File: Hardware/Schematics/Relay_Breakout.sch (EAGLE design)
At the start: 63 parts, among them U1 ESP-32S

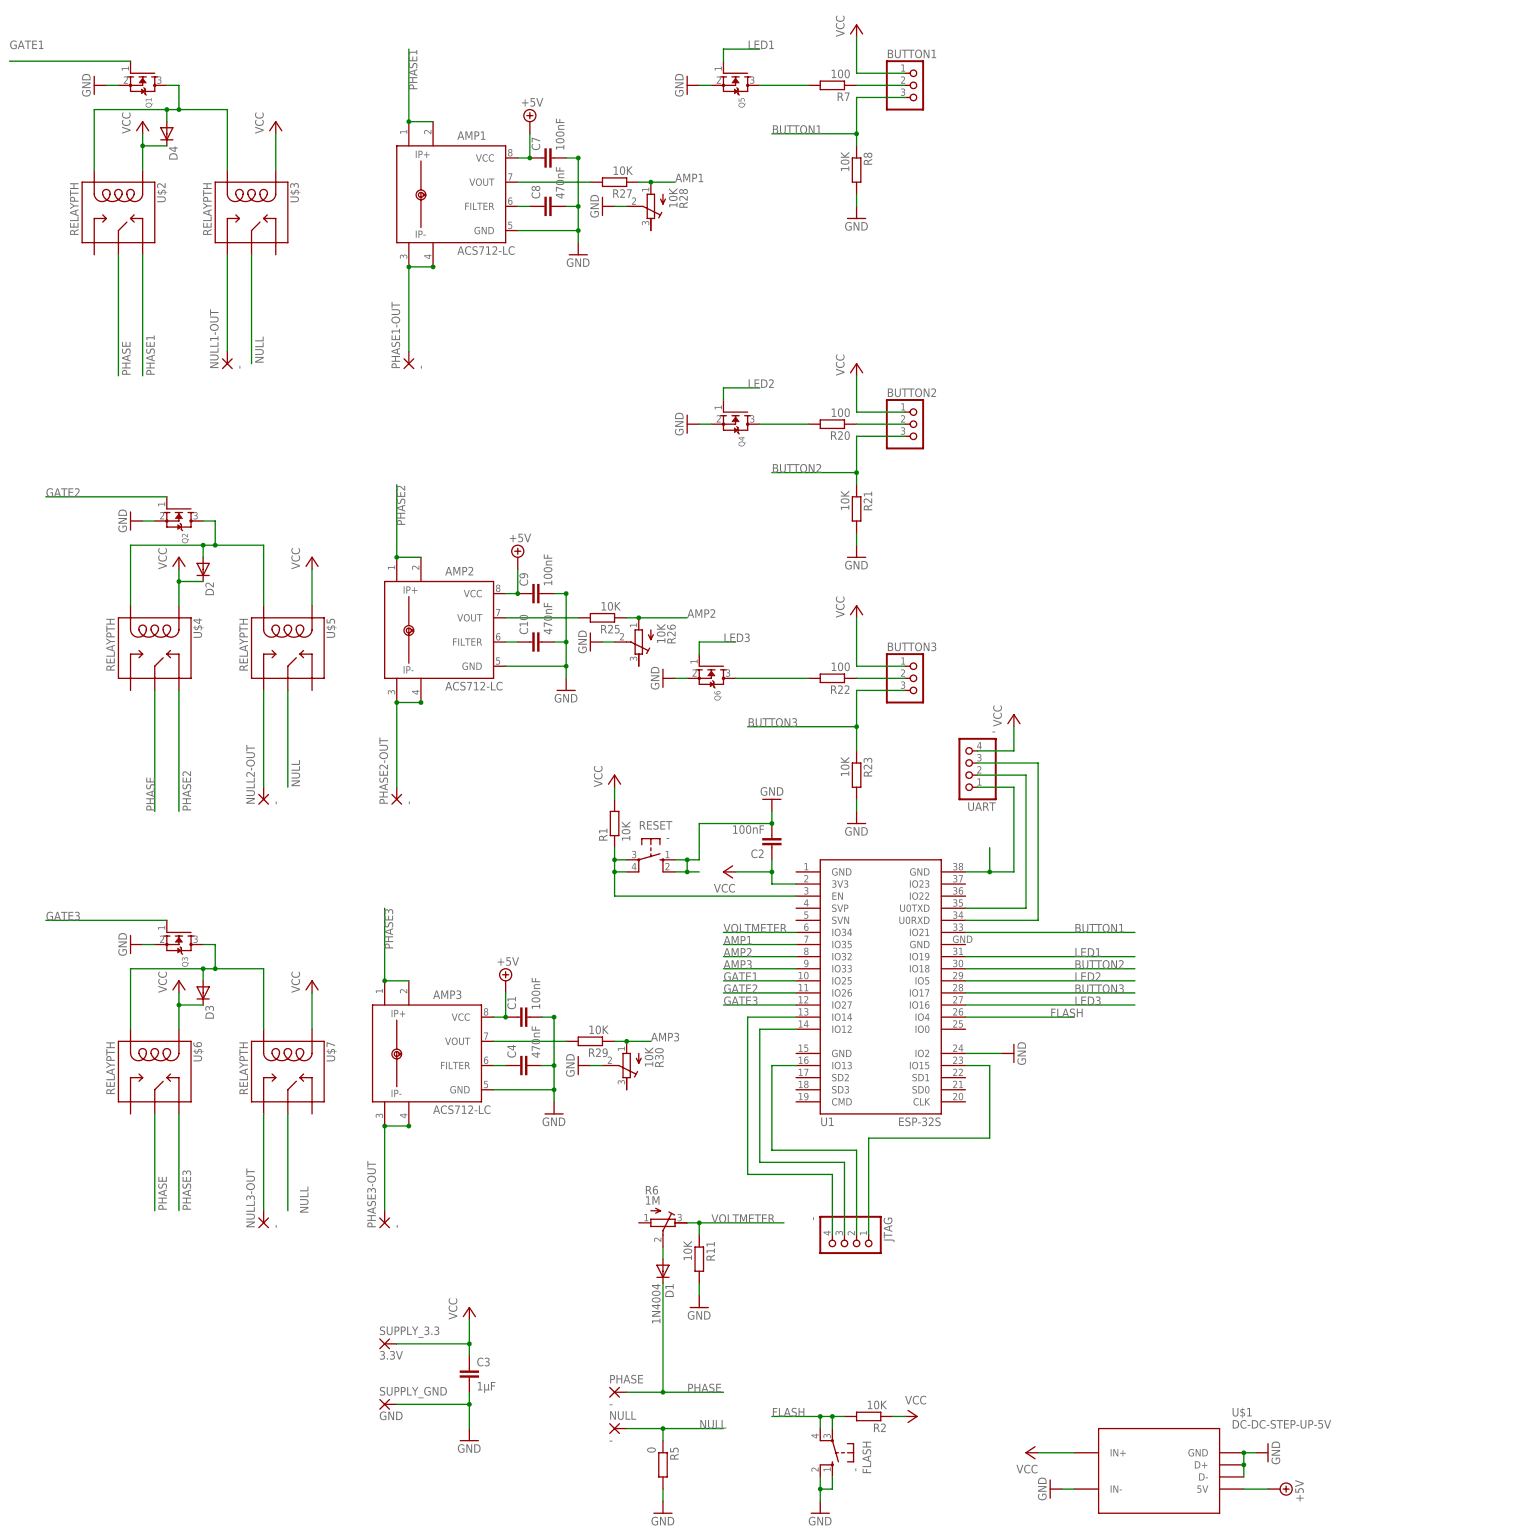
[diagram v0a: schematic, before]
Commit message: Made relay and amperemeter breakout board.
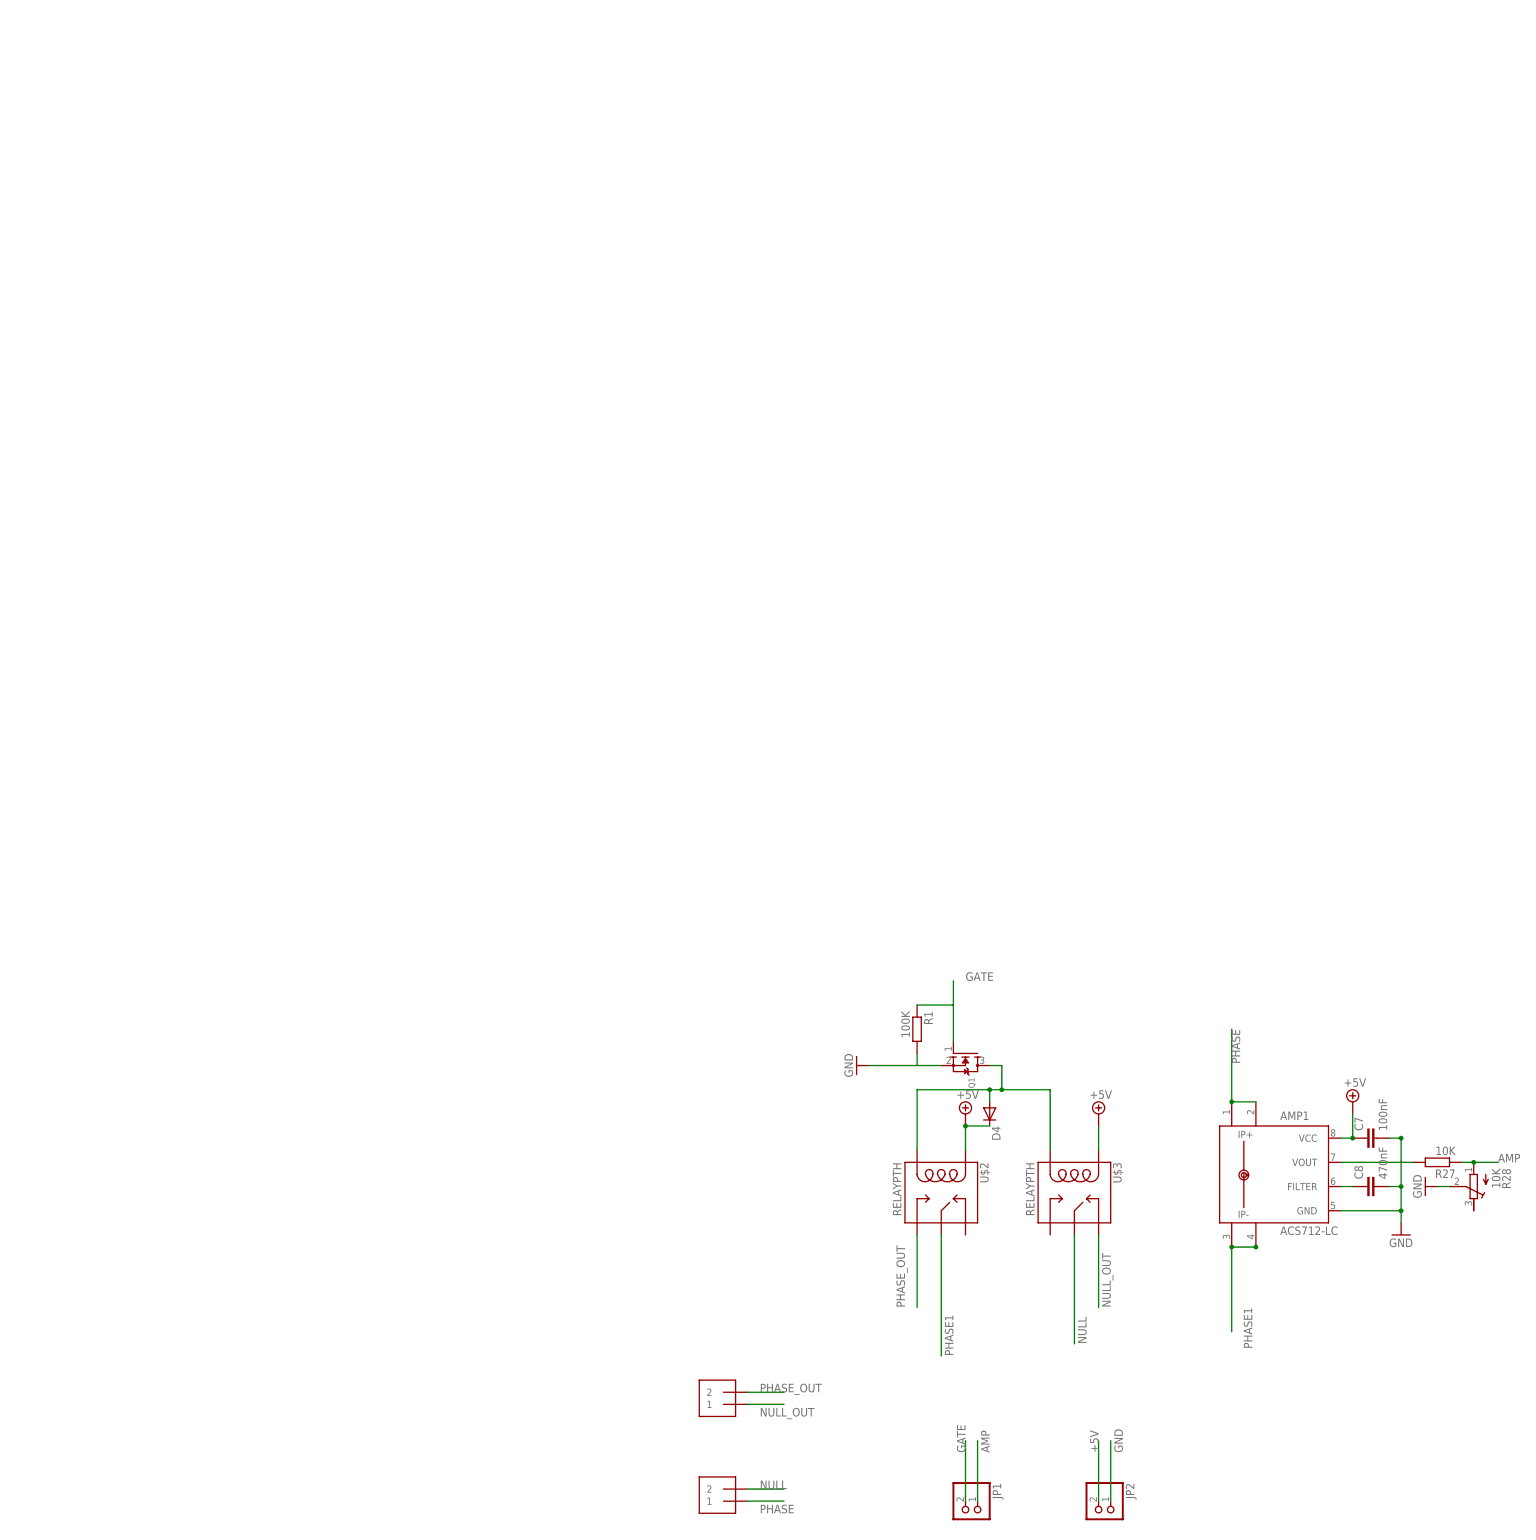
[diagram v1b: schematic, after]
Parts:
- removed AMP2, AMP3: ACS712-LC, allegro-2:ACS712-LC
- removed BUTTON1, BUTTON2, BUTTON3: (no value), pinhead:PINHD-1X3
- removed C1, C9: 100nF, rcl:C-EUC0805
- removed C10, C4: 470nF, rcl:C-EUC0805
- removed C2: 100nF, rcl:C-EUC1206
- removed C3: 1µF, rcl:C-EU025-024X044
- removed D1: 1N4004, diode:1N4004
- removed D2, D3: (no value), diode:DIODE-DO-214AC
- removed FLASH, RESET: -, switch-omron:10-XX
- removed JTAG, UART: -, pinhead:PINHD-1X4
- removed NULL, NULL1-OUT, NULL2-OUT, NULL3-OUT, PHASE, PHASE1-OUT, PHASE2-OUT, PHASE3-OUT: -, wirepad:3,81/1,4
- removed Q2, Q3, Q4, Q5, Q6: (no value), adafruit:MOSFET-NREFLOW
- removed R11, R2, R21, R23, R25, R29, R8: 10K, rcl:R-EU_R0805
- removed R20, R22, R7: 100, rcl:R-EU_R0805
- removed R26, R30: 10K, rcl:R-TRIMM5X
- removed R5: 0, eagle-ltspice:RR2010
- removed R6: 1M, rcl:R-TRIMM3296W
- removed SUPPLY_3.3: 3.3V, wirepad:2,15/1,0
- removed SUPPLY_GND: GND, wirepad:2,15/1,0
- removed U$1: DC-DC-STEP-UP-5V, diy-modules:DC-DC-STEP-UP-5V
- removed U$4, U$5, U$6, U$7: RELAYPTH, SRD-05VDC-SL-C:RELAYPTH
- removed U1: ESP-32S, esp32:ESP-32S
- added J1, J2: 1X2-3.5MM, adafruit:1X2-3.5MM
- added JP1, JP2: (no value), pinhead:PINHD-1X2
- R1: value 10K -> 100K
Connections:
- removed net AMP1: R27.1, R28.A, U1.IO35
- removed net AMP2: R25.1, R26.A, U1.IO32
- removed net AMP3: R29.1, R30.A, U1.IO33
- removed net BUTTON1: BUTTON1.3, R8.1, U1.IO21
- removed net BUTTON2: BUTTON2.3, R21.1, U1.IO18
- removed net BUTTON3: BUTTON3.3, R23.1, U1.IO17
- removed net FLASH: FLASH.P, FLASH.P1, R2.2, U1.IO4
- removed net GATE1: Q1.G, U1.IO25
- removed net GATE2: Q2.G, U1.IO26
- removed net GATE3: Q3.G, U1.IO27
- removed net LED1: Q5.G, U1.IO19
- removed net LED1_SWITCHED: Q5.D, R7.2
- removed net LED2: Q4.G, U1.IO5
- removed net LED2_SWITCHED: Q4.D, R20.2
- removed net LED3: Q6.G, U1.IO16
- removed net LED3_SWITCHED: Q6.D, R22.2
- removed net N$10: AMP3.IP-, AMP3.IP-1, PHASE3-OUT.P
- removed net N$11: BUTTON3.2, R22.1
- removed net N$12: AMP2.IP-, AMP2.IP-1, PHASE2-OUT.P
- removed net N$13: AMP2.FILTER, C10.1
- removed net N$14: D2.A, Q2.D, U$4.COIL0, U$5.COIL0
- removed net N$17: NULL2-OUT.P, U$5.SWOPEN
- removed net N$19: U1.GND@3, UART.1
- removed net N$26: AMP3.FILTER, C4.1
- removed net N$27: AMP1.IP-, AMP1.IP-1, PHASE1-OUT.P
- removed net N$3: JTAG.2, U1.IO13
- removed net N$37: AMP3.VOUT, R29.2
- removed net N$39: AMP2.VOUT, R25.2
- removed net N$4: JTAG.3, U1.IO12
- removed net N$42: D1.A, R6.S
- removed net N$5: JTAG.4, U1.IO14
- removed net N$6: D3.A, Q3.D, U$6.COIL0, U$7.COIL0
- removed net N$66: R1.1, RESET.P, RESET.P1, U1.EN
- removed net N$7: BUTTON2.2, R20.1
- removed net N$70: U1.U0TXD, UART.2
- removed net N$77: U1.U0RXD, UART.3
- removed net N$8: NULL1-OUT.P, U$3.SWOPEN
- removed net N$9: BUTTON1.2, R7.1
- removed net NULL_: NULL3-OUT.P, U$7.SWOPEN
- removed net PHASE2: AMP2.IP+, AMP2.IP+1, U$4.SWCLOSE
- removed net PHASE3: AMP3.IP+, AMP3.IP+1, U$6.SWCLOSE
- removed net VCC: BUTTON1.1, BUTTON2.1, BUTTON3.1, C2.1, C3.1, D2.C, D3.C, D4.C, R1.2, R2.1, SUPPLY_3.3.P, U$1.IN+, U$2.COIL1, U$3.COIL1, U$4.COIL1, U$5.COIL1, U$6.COIL1, U$7.COIL1, U1.3V3, UART.4
- removed net VOLTMETER: R11.1, R6.E, U1.IO34
- new net AMP: JP1.1, R27.1, R28.A
- new net GATE: JP1.2, Q1.G, R1.1
- new net NULL_OUT: J2.1, U$3.SWCLOSE
- new net PHASE_OUT: J2.2, U$2.SWOPEN
- net +5V: now also JP2.2, U$3.COIL1; no longer AMP2.VCC, AMP3.VCC, C1.1, C9.1, U$1.5V
- net GND: now also JP2.1, R1.2; no longer AMP2.GND, AMP3.GND, C1.2, C10.2, C2.2, C3.2, C4.2, C9.2, FLASH.S, FLASH.S1, Q2.S, Q3.S, Q4.S, Q5.S, Q6.S, R11.2, R21.2, R23.2, R26.S, R30.S, R5.2, R8.2, RESET.S, RESET.S1, SUPPLY_GND.P, U$1.D+, U$1.D-, U$1.GND, U$1.IN-, U1.IO2
- net N$2: now also D4.C, U$2.COIL1; no longer JTAG.1, U1.IO15
- net NULL: now also J1.2; no longer NULL.P, R5.1, U$5.SWCOMMON, U$7.SWCOMMON
- net PHASE: now also AMP1.IP+, AMP1.IP+1, J1.1; no longer D1.C, PHASE.P, U$2.SWCOMMON, U$4.SWCOMMON, U$6.SWCOMMON
- net PHASE1: now also AMP1.IP-, AMP1.IP-1, U$2.SWCOMMON; no longer AMP1.IP+, AMP1.IP+1, U$2.SWCLOSE
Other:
- moved on the sheet: AMP1, C7, C8, D4, Q1, R1, R27, R28, U$2, U$3

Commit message: fixed some issues in relay breakout.
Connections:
- removed net N$2: D4.C, U$2.COIL1
- net +5V: now also D4.C, U$2.COIL1
- net PHASE_OUT: now also U$2.SWCLOSE; no longer U$2.SWOPEN
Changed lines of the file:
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@@
 <part name="J2" library="adafruit" deviceset="1X2" device="-3.5MM"/>
 <part name="P+1" library="supply2" deviceset="+5V" device=""/>
-<part name="P+2" library="supply2" deviceset="+5V" device=""/>
 <part name="R1" library="rcl" deviceset="R-EU_" device="R0805" value="100K"/>
 <part name="JP1" library="pinhead" deviceset="PINHD-1X2" device=""/>
 <part name="JP2" library="pinhead" deviceset="PINHD-1X2" device=""/>
+<part name="P+2" library="supply2" deviceset="+5V" device=""/>
 </parts>
 <sheets>
@@
 <instance part="J2" gate="G$1" x="-22.86" y="-35.56" rot="R180"/>
 <instance part="P+1" gate="+5V" x="55.88" y="22.86"/>
-<instance part="P+2" gate="+5V" x="27.94" y="22.86"/>
 <instance part="R1" gate="G$1" x="17.78" y="40.64" rot="R270"/>
 <instance part="JP1" gate="G$1" x="27.94" y="-60.96" rot="R270"/>
 <instance part="JP2" gate="G$1" x="55.88" y="-60.96" rot="R270"/>
+<instance part="P+2" gate="+5V" x="27.94" y="22.86"/>
 </instances>
 <busses>
@@
 <wire x1="17.78" y1="33.02" x2="7.62" y2="33.02" width="0.1524" layer="91"/>
 <wire x1="17.78" y1="35.56" x2="17.78" y2="33.02" width="0.1524" layer="91"/>
+<junction x="17.78" y="33.02"/>
 </segment>
 <segment>
@@
 <wire x1="25.4" y1="45.72" x2="25.4" y2="50.8" width="0.1524" layer="91"/>
 <wire x1="17.78" y1="45.72" x2="25.4" y2="45.72" width="0.1524" layer="91"/>
+<junction x="25.4" y="45.72"/>
 </segment>
 <segment>
@@
 </segment>
 <segment>
-<pinref part="U$2" gate="G$1" pin="SWOPEN"/>
-<wire x1="17.78" y1="-2.54" x2="17.78" y2="-17.78" width="0.1524" layer="91"/>
-<label x="15.24" y="-17.78" size="1.778" layer="95" rot="R90"/>
+<pinref part="U$2" gate="G$1" pin="SWCLOSE"/>
+<wire x1="27.94" y1="-2.54" x2="27.94" y2="-27.94" width="0.1524" layer="91"/>
+<label x="30.48" y="-27.94" size="1.778" layer="95" rot="R90"/>
 </segment>
 </net>
@@
 <wire x1="55.88" y1="-58.42" x2="55.88" y2="-45.72" width="0.1524" layer="91"/>
 <label x="55.88" y="-48.26" size="1.778" layer="95" rot="R90"/>
+</segment>
+<segment>
+<pinref part="U$2" gate="G$1" pin="COIL1"/>
+<wire x1="27.94" y1="17.78" x2="27.94" y2="15.24" width="0.1524" layer="91"/>
+<pinref part="D4" gate="G$1" pin="C"/>
+<wire x1="33.02" y1="20.32" x2="33.02" y2="17.78" width="0.1524" layer="91"/>
+<wire x1="33.02" y1="17.78" x2="27.94" y2="17.78" width="0.1524" layer="91"/>
+<pinref part="P+2" gate="+5V" pin="+5V"/>
+<wire x1="27.94" y1="17.78" x2="27.94" y2="20.32" width="0.1524" layer="91"/>
+<junction x="27.94" y="17.78"/>
 </segment>
 </net>
@@
 </segment>
 </net>
-<net name="N$2" class="0">
-<segment>
-<pinref part="U$2" gate="G$1" pin="COIL1"/>
-<pinref part="D4" gate="G$1" pin="C"/>
-<wire x1="27.94" y1="20.32" x2="27.94" y2="15.24" width="0.1524" layer="91"/>
-<wire x1="33.02" y1="20.32" x2="27.94" y2="20.32" width="0.1524" layer="91"/>
-<junction x="27.94" y="20.32"/>
-<pinref part="P+2" gate="+5V" pin="+5V"/>
-</segment>
-</net>
 </nets>
 </sheet>
 </sheets>
+<errors>
+</errors>
 </schematic>
 </drawing>

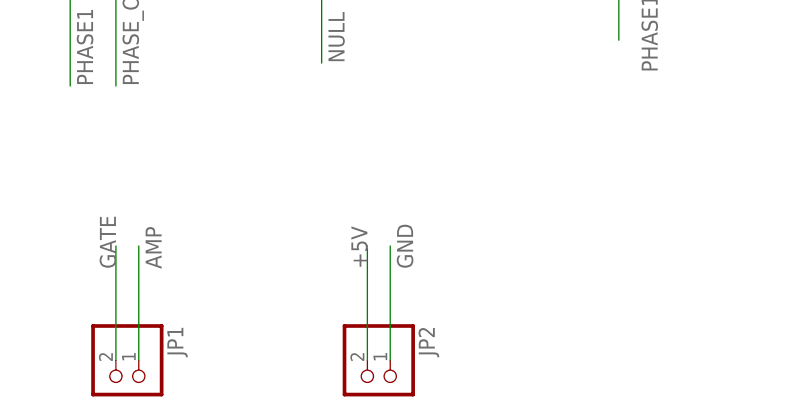
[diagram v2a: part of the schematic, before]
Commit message: Routed power socket board.
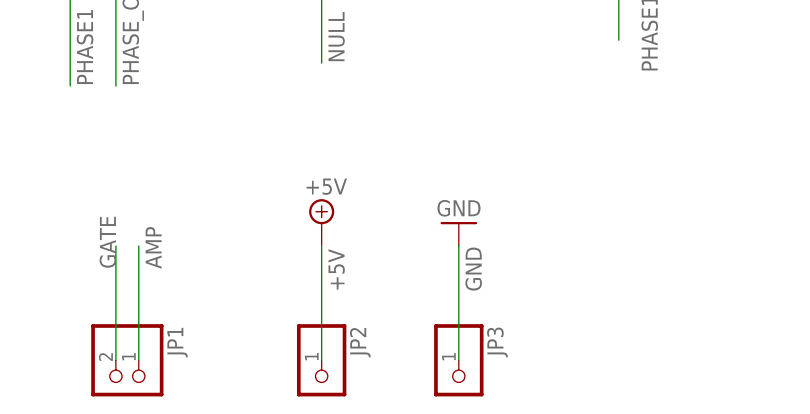
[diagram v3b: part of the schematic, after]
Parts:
- added JP3: (no value), pinhead:PINHD-1X1
- JP2: device pinhead:PINHD-1X2 -> pinhead:PINHD-1X1
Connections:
- net +5V: now also JP2.1; no longer JP2.2
- net GND: now also JP3.1; no longer JP2.1
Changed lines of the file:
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@@
 <part name="J1" library="adafruit" deviceset="1X2" device="-3.5MM"/>
 <part name="J2" library="adafruit" deviceset="1X2" device="-3.5MM"/>
-<part name="P+1" library="supply2" deviceset="+5V" device=""/>
+<part name="COPT" library="supply2" deviceset="+5V" device=""/>
 <part name="R1" library="rcl" deviceset="R-EU_" device="R0805" value="100K"/>
 <part name="JP1" library="pinhead" deviceset="PINHD-1X2" device=""/>
-<part name="JP2" library="pinhead" deviceset="PINHD-1X2" device=""/>
 <part name="P+2" library="supply2" deviceset="+5V" device=""/>
+<part name="JP2" library="pinhead" deviceset="PINHD-1X1" device=""/>
+<part name="JP3" library="pinhead" deviceset="PINHD-1X1" device=""/>
+<part name="COPT1" library="supply2" deviceset="+5V" device=""/>
+<part name="GND1" library="supply1" deviceset="GND" device=""/>
 </parts>
 <sheets>
@@
 <instance part="J1" gate="G$1" x="-22.86" y="-55.88" rot="R180"/>
 <instance part="J2" gate="G$1" x="-22.86" y="-35.56" rot="R180"/>
-<instance part="P+1" gate="+5V" x="55.88" y="22.86"/>
+<instance part="COPT" gate="+5V" x="55.88" y="22.86"/>
 <instance part="R1" gate="G$1" x="17.78" y="40.64" rot="R270"/>
 <instance part="JP1" gate="G$1" x="27.94" y="-60.96" rot="R270"/>
-<instance part="JP2" gate="G$1" x="55.88" y="-60.96" rot="R270"/>
 <instance part="P+2" gate="+5V" x="27.94" y="22.86"/>
+<instance part="JP2" gate="G$1" x="50.8" y="-60.96" rot="R270"/>
+<instance part="JP3" gate="G$1" x="66.04" y="-60.96" rot="R270"/>
+<instance part="COPT1" gate="+5V" x="50.8" y="-43.18"/>
+<instance part="GND1" gate="1" x="66.04" y="-43.18" rot="R180"/>
 </instances>
 <busses>
@@
 </segment>
 <segment>
-<pinref part="JP2" gate="G$1" pin="1"/>
-<wire x1="58.42" y1="-58.42" x2="58.42" y2="-45.72" width="0.1524" layer="91"/>
-<label x="60.96" y="-48.26" size="1.778" layer="95" rot="R90"/>
+<pinref part="JP3" gate="G$1" pin="1"/>
+<wire x1="66.04" y1="-58.42" x2="66.04" y2="-45.72" width="0.1524" layer="91"/>
+<label x="68.58" y="-50.8" size="1.778" layer="95" rot="R90"/>
+<pinref part="GND1" gate="1" pin="GND"/>
 </segment>
 </net>
@@
 <pinref part="U$3" gate="G$1" pin="COIL1"/>
 <wire x1="55.88" y1="20.32" x2="55.88" y2="15.24" width="0.1524" layer="91"/>
-<pinref part="P+1" gate="+5V" pin="+5V"/>
-</segment>
-<segment>
-<pinref part="JP2" gate="G$1" pin="2"/>
-<wire x1="55.88" y1="-58.42" x2="55.88" y2="-45.72" width="0.1524" layer="91"/>
-<label x="55.88" y="-48.26" size="1.778" layer="95" rot="R90"/>
+<pinref part="COPT" gate="+5V" pin="+5V"/>
 </segment>
 <segment>
@@
 <junction x="27.94" y="17.78"/>
 </segment>
-</net>
+<segment>
+<pinref part="JP2" gate="G$1" pin="1"/>
+<wire x1="50.8" y1="-58.42" x2="50.8" y2="-45.72" width="0.1524" layer="91"/>
+<label x="53.34" y="-50.8" size="1.778" layer="95" rot="R90"/>
+<pinref part="COPT1" gate="+5V" pin="+5V"/>
+</segment>
+</net>
